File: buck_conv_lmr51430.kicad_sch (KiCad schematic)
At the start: 10 parts, among them J1 Screw_Terminal_01x02, J2 Screw_Terminal_01x02

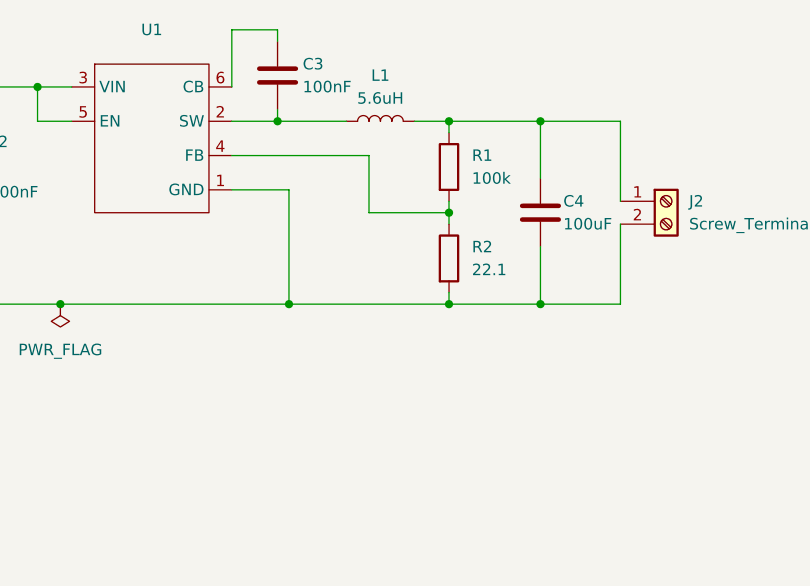
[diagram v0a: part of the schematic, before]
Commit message: Add variable output feedback network
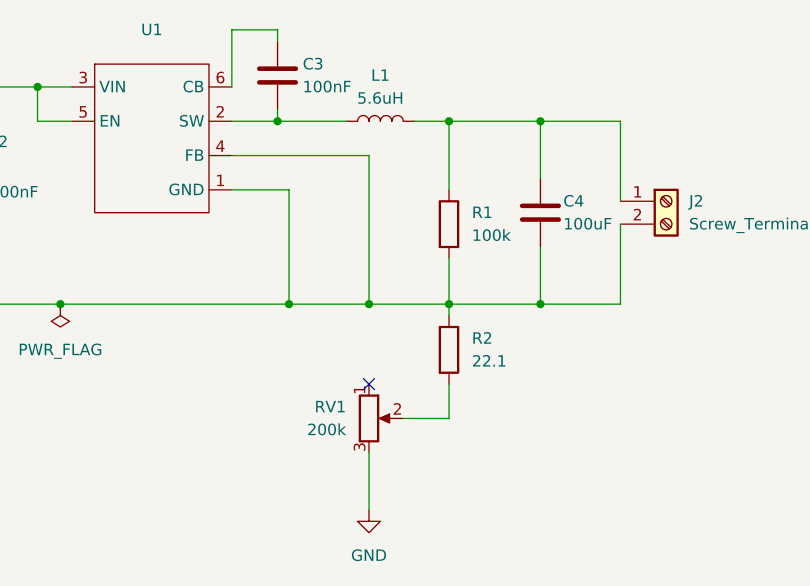
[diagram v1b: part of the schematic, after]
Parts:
- added RV1: 200k, Potentiometer_THT:Potentiometer_Bourns_3266Y_Vertical, symbol Device:R_Potentiometer
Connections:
- net GND: now also R1.2, R2.1, U1.4 (FB), RV1.3; no longer R2.2
- new net: R2.2, RV1.2
- no-connect marks 0 -> 1
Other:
- moved on the sheet: R1, R2
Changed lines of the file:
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@@
 	(paper "A4")
+	(junction
+		(at 102.87 123.19)
+		(diameter 0)
+		(color 0 0 0 0)
+	)
+	(junction
+		(at 165.1 123.19)
+		(diameter 0)
+		(color 0 0 0 0)
+	)
 	(junction
 		(at 175.26 123.19)
@@
 	)
 	(junction
-		(at 102.87 123.19)
-		(diameter 0)
-		(color 0 0 0 0)
-	)
-	(junction
 		(at 175.26 102.87)
 		(diameter 0)
@@
 	)
 	(junction
-		(at 165.1 113.03)
-		(diameter 0)
-		(color 0 0 0 0)
-	)
-	(junction
 		(at 111.76 99.06)
 		(diameter 0)
@@
 	)
 	(junction
-		(at 165.1 123.19)
+		(at 147.32 123.19)
 		(diameter 0)
 		(color 0 0 0 0)
@@
 	)
 	(junction
-		(at 147.32 123.19)
+		(at 156.21 123.19)
 		(diameter 0)
 		(color 0 0 0 0)
@@
 		(color 0 0 0 0)
 	)
+	(no_connect
+		(at 156.21 132.08)
+	)
 	(wire
 		(pts
@@
 	(wire
 		(pts
-			(xy 165.1 113.03) (xy 165.1 114.3)
+			(xy 156.21 139.7) (xy 156.21 146.05)
+		)
+		(stroke
+			(width 0)
+			(type default)
+		)
+	)
+	(wire
+		(pts
+			(xy 165.1 123.19) (xy 175.26 123.19)
+		)
+		(stroke
+			(width 0)
+			(type default)
+		)
+	)
+	(wire
+		(pts
+			(xy 156.21 123.19) (xy 147.32 123.19)
 		)
 		(stroke
@@
 	(wire
 		(pts
-			(xy 165.1 123.19) (xy 175.26 123.19)
+			(xy 165.1 135.89) (xy 160.02 135.89)
 		)
 		(stroke
@@
 	(wire
 		(pts
+			(xy 165.1 123.19) (xy 165.1 124.46)
+		)
+		(stroke
+			(width 0)
+			(type default)
+		)
+	)
+	(wire
+		(pts
 			(xy 165.1 102.87) (xy 175.26 102.87)
 		)
@@
 	(wire
 		(pts
-			(xy 165.1 102.87) (xy 165.1 104.14)
+			(xy 165.1 102.87) (xy 165.1 110.49)
 		)
 		(stroke
@@
 	(wire
 		(pts
-			(xy 165.1 123.19) (xy 165.1 121.92)
-		)
-		(stroke
-			(width 0)
-			(type default)
-		)
-	)
-	(wire
-		(pts
 			(xy 140.97 102.87) (xy 146.05 102.87)
 		)
@@
 	(wire
 		(pts
+			(xy 165.1 132.08) (xy 165.1 135.89)
+		)
+		(stroke
+			(width 0)
+			(type default)
+		)
+	)
+	(wire
+		(pts
 			(xy 123.19 102.87) (xy 119.38 102.87)
 		)
@@
 	(wire
 		(pts
-			(xy 165.1 111.76) (xy 165.1 113.03)
+			(xy 165.1 118.11) (xy 165.1 123.19)
 		)
 		(stroke
@@
 	(wire
 		(pts
-			(xy 156.21 113.03) (xy 165.1 113.03)
+			(xy 156.21 123.19) (xy 165.1 123.19)
 		)
 		(stroke
@@
 	(wire
 		(pts
-			(xy 156.21 106.68) (xy 156.21 113.03)
-		)
-		(stroke
-			(width 0)
-			(type default)
-		)
-	)
-	(wire
-		(pts
 			(xy 175.26 102.87) (xy 184.15 102.87)
 		)
@@
 	(wire
 		(pts
+			(xy 156.21 106.68) (xy 156.21 123.19)
+		)
+		(stroke
+			(width 0)
+			(type default)
+		)
+	)
+	(wire
+		(pts
 			(xy 184.15 123.19) (xy 175.26 123.19)
 		)
@@
 		(pts
 			(xy 184.15 102.87) (xy 184.15 111.76)
-		)
-		(stroke
-			(width 0)
-			(type default)
-		)
-	)
-	(wire
-		(pts
-			(xy 147.32 123.19) (xy 165.1 123.19)
 		)
 		(stroke
@@
 	)
 	(symbol
+		(lib_id "power:GND")
+		(at 156.21 146.05 0)
+		(unit 1)
+		(exclude_from_sim no)
+		(in_bom yes)
+		(on_board yes)
+		(dnp no)
+		(fields_autoplaced yes)
+		(property "Reference" "#PWR02"
+			(at 156.21 152.4 0)
+			(effects
+				(font
+					(size 1.27 1.27)
+				)
+				(hide yes)
+			)
+		)
+		(property "Value" "GND"
+			(at 156.21 151.13 0)
+			(effects
+				(font
+					(size 1.27 1.27)
+				)
+			)
+		)
+		(property "Footprint" ""
+			(at 156.21 146.05 0)
+			(effects
+				(font
+					(size 1.27 1.27)
+				)
+				(hide yes)
+			)
+		)
+		(property "Datasheet" ""
+			(at 156.21 146.05 0)
+			(effects
+				(font
+					(size 1.27 1.27)
+				)
+				(hide yes)
+			)
+		)
+		(property "Description" "Power symbol creates a global label with name \"GND\" , ground"
+			(at 156.21 146.05 0)
+			(effects
+				(font
+					(size 1.27 1.27)
+				)
+				(hide yes)
+			)
+		)
+		(pin "1"
+		)
+		(instances
+			(project ""
+				(path "/26cd2869-c290-408a-9b2f-5ee5b71a4927"
+					(reference "#PWR02")
+					(unit 1)
+				)
+			)
+		)
+	)
+	(symbol
 		(lib_id "Device:C")
 		(at 175.26 113.03 0)
@@
 	(symbol
 		(lib_id "Device:R")
-		(at 165.1 107.95 0)
+		(at 165.1 114.3 0)
 		(unit 1)
 		(exclude_from_sim no)
@@
 		(fields_autoplaced yes)
 		(property "Reference" "R1"
-			(at 167.64 106.6799 0)
+			(at 167.64 113.0299 0)
 			(effects
 				(font
@@
 		)
 		(property "Value" "100k"
-			(at 167.64 109.2199 0)
+			(at 167.64 115.5699 0)
 			(effects
 				(font
@@
 		)
 		(property "Footprint" "Resistor_THT:R_Axial_DIN0204_L3.6mm_D1.6mm_P5.08mm_Horizontal"
-			(at 163.322 107.95 90)
+			(at 163.322 114.3 90)
 			(effects
 				(font
@@
 		)
 		(property "Datasheet" "~"
-			(at 165.1 107.95 0)
+			(at 165.1 114.3 0)
 			(effects
 				(font
@@
 		)
 		(property "Description" "Resistor"
-			(at 165.1 107.95 0)
+			(at 165.1 114.3 0)
 			(effects
 				(font
@@
 	)
 	(symbol
+		(lib_id "Device:R_Potentiometer")
+		(at 156.21 135.89 0)
+		(unit 1)
+		(exclude_from_sim no)
+		(in_bom yes)
+		(on_board yes)
+		(dnp no)
+		(fields_autoplaced yes)
+		(property "Reference" "RV1"
+			(at 153.67 134.6199 0)
+			(effects
+				(font
+					(size 1.27 1.27)
+				)
+				(justify right)
+			)
+		)
+		(property "Value" "200k"
+			(at 153.67 137.1599 0)
+			(effects
+				(font
+					(size 1.27 1.27)
+				)
+				(justify right)
+			)
+		)
+		(property "Footprint" "Potentiometer_THT:Potentiometer_Bourns_3266Y_Vertical"
+			(at 156.21 135.89 0)
+			(effects
+				(font
+					(size 1.27 1.27)
+				)
+				(hide yes)
+			)
+		)
+		(property "Datasheet" "~"
+			(at 156.21 135.89 0)
+			(effects
+				(font
+					(size 1.27 1.27)
+				)
+				(hide yes)
+			)
+		)
+		(property "Description" "Potentiometer"
+			(at 156.21 135.89 0)
+			(effects
+				(font
+					(size 1.27 1.27)
+				)
+				(hide yes)
+			)
+		)
+		(pin "3"
+		)
+		(pin "2"
+		)
+		(pin "1"
+		)
+		(instances
+			(project ""
+				(path "/26cd2869-c290-408a-9b2f-5ee5b71a4927"
+					(reference "RV1")
+					(unit 1)
+				)
+			)
+		)
+	)
+	(symbol
 		(lib_id "Device:R")
-		(at 165.1 118.11 0)
+		(at 165.1 128.27 0)
 		(unit 1)
 		(exclude_from_sim no)
@@
 		(fields_autoplaced yes)
 		(property "Reference" "R2"
-			(at 167.64 116.8399 0)
+			(at 167.64 126.9999 0)
 			(effects
 				(font
@@
 		)
 		(property "Value" "22.1"
-			(at 167.64 119.3799 0)
+			(at 167.64 129.5399 0)
 			(effects
 				(font
@@
 		)
 		(property "Footprint" "Resistor_THT:R_Axial_DIN0204_L3.6mm_D1.6mm_P5.08mm_Horizontal"
-			(at 163.322 118.11 90)
+			(at 163.322 128.27 90)
 			(effects
 				(font
@@
 		)
 		(property "Datasheet" "~"
-			(at 165.1 118.11 0)
+			(at 165.1 128.27 0)
 			(effects
 				(font
@@
 		)
 		(property "Description" "Resistor"
-			(at 165.1 118.11 0)
-			(effects
-				(font
+			(at 165.1 128.27 0)
+			(effects
+				(font

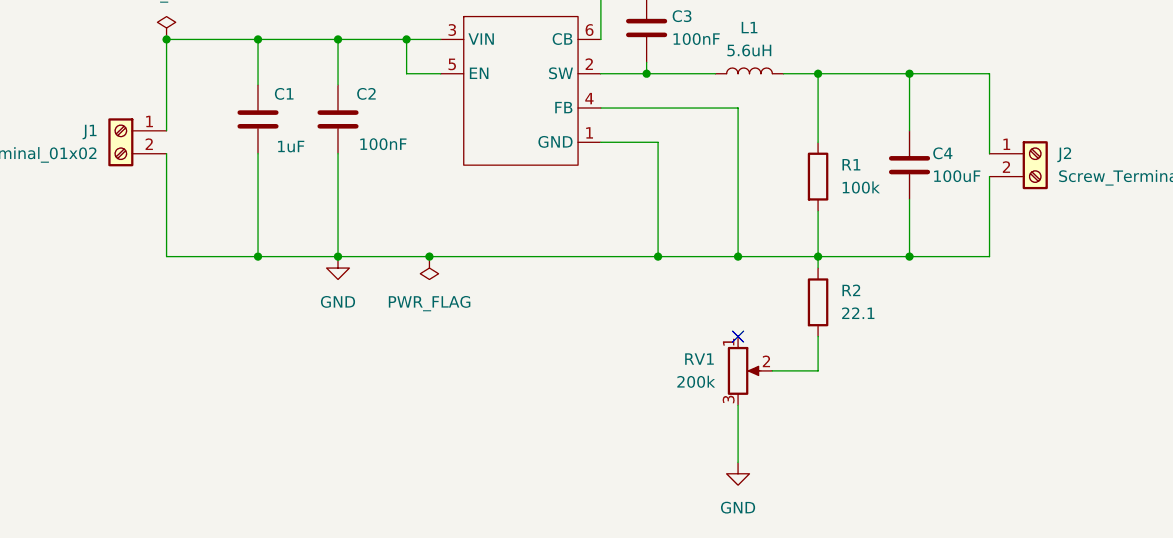
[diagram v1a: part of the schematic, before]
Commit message: Inductor selection and footprint fix
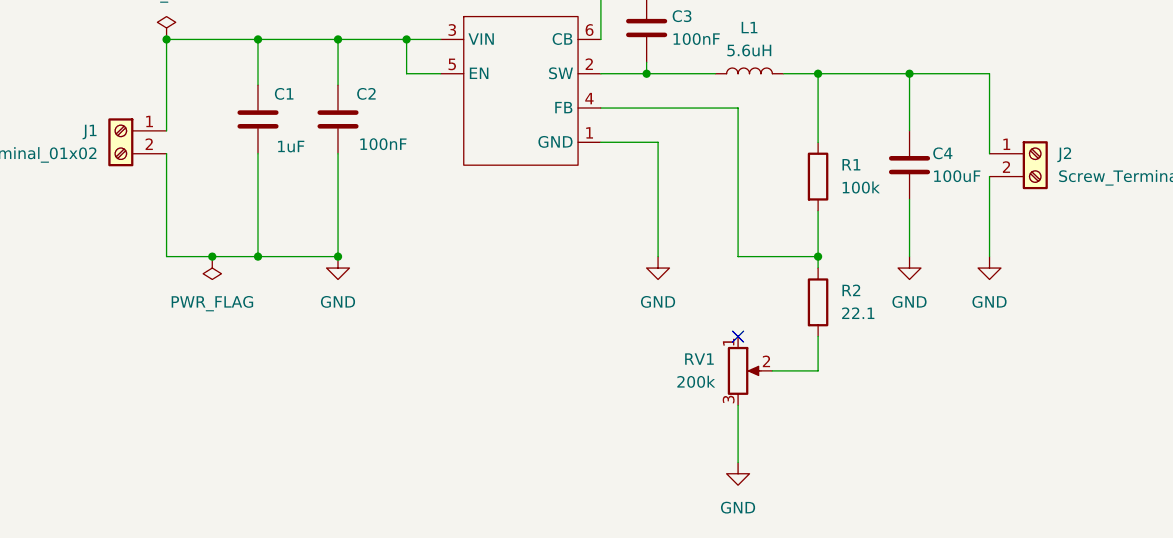
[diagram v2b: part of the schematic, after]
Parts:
- L1: footprint Inductor_SMD:L_7.3x7.3_H4.5 -> Inductor_SMD:L_APV_APH1030
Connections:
- net GND: no longer R1.2, R2.1, U1.4 (FB)
- new net: R1.2, R2.1, U1.4 (FB)

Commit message: rajath final touches
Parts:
- removed U1: ~, Package_TO_SOT_SMD:SOT-23-6, symbol LMR51430:LMR51430
- added C5, C6: 22u, Capacitor_SMD:C_0805_2012Metric_Pad1.18x1.45mm_HandSolder, symbol Device:C
- added U1: LMR51430, Package_TO_SOT_SMD:SOT-23-6, symbol Regulator_Switching:LMR51430
- C1: value 1uF -> 4.7u; footprint Capacitor_SMD:C_0805_2012Metric -> Capacitor_SMD:C_0805_2012Metric_Pad1.18x1.45mm_HandSolder
- C2: value 100nF -> 100n; footprint Capacitor_SMD:C_0805_2012Metric -> Capacitor_SMD:C_0805_2012Metric_Pad1.18x1.45mm_HandSolder
- C3: value 100nF -> 100n; footprint Capacitor_SMD:C_0603_1608Metric -> Capacitor_SMD:C_0805_2012Metric_Pad1.18x1.45mm_HandSolder
- C4: value 100uF -> 22u; footprint Capacitor_THT:CP_Radial_D6.3mm_P2.50mm -> Capacitor_SMD:C_0805_2012Metric_Pad1.18x1.45mm_HandSolder
- J1: value Screw_Terminal_01x02 -> Input
- J2: value Screw_Terminal_01x02 -> Output
- L1: value 5.6uH -> 12u
- R1: value 100k -> 100K; footprint Resistor_THT:R_Axial_DIN0204_L3.6mm_D1.6mm_P5.08mm_Horizontal -> Resistor_SMD:R_0805_2012Metric_Pad1.20x1.40mm_HandSolder
- R2: value 22.1 -> 5K; footprint Resistor_THT:R_Axial_DIN0204_L3.6mm_D1.6mm_P5.08mm_Horizontal -> Resistor_SMD:R_0805_2012Metric_Pad1.20x1.40mm_HandSolder
- RV1: value 200k -> 20K
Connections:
- net GND: now also J2.1 (Pin_1), C5.2, C6.2, U1.1 (GND); no longer J2.2 (Pin_2)
- net SW: now reaches C3.2, L1.1
- net SW: now also U1.2 (SW)
- net VIN: now reaches C1.1, C2.1, J1.1 (Pin_1)
- net VIN: now also U1.3 (VIN), U1.5 (EN)
- net FB: now reaches R1.2, R2.1
- net FB: now also U1.4 (FB)
- net at C3.1: now also U1.6 (CB)
- net VOUT: now reaches C4.1, L1.2, R1.1
- net VOUT: now also J2.2 (Pin_2), C5.1, C6.1; no longer J2.1 (Pin_1)
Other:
- note added: "DC-DC Buck Converter"
- note added: "Note - All the capacitors should be Cermaic capacitor Input capacitors C1, C2, C3 should be rated for 50V Ouput capacitors C4, C5, C6 should be rated for 25V Inductor should saturation current should be above 5A"
- title: (none) -> DC-DC Buck Converter
